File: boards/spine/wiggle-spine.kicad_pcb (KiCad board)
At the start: 2 copper layers, 114.3 x 88.9 mm, 187 parts, among them CON1 USB-B, CON2 XLR-3 Female, CON3 USB-A, CON4 2.5mm 5-24V 5A, CON5 5-24V 16A, CON6 PLR135, CON7 PLT133, Q1 DMN3190LDW, Q2 2N7002P, Q3 AOD4189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

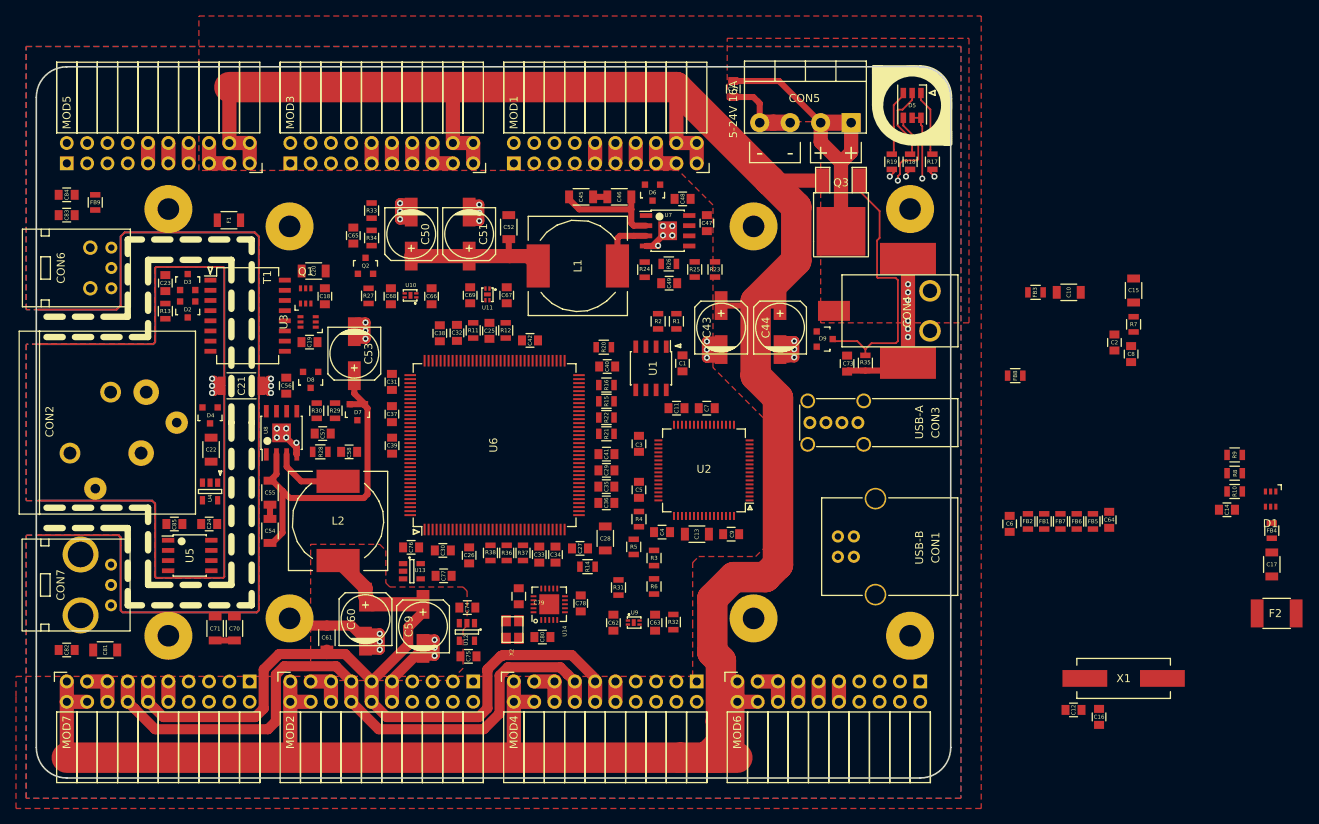
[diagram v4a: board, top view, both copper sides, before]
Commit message: Working on module power routing
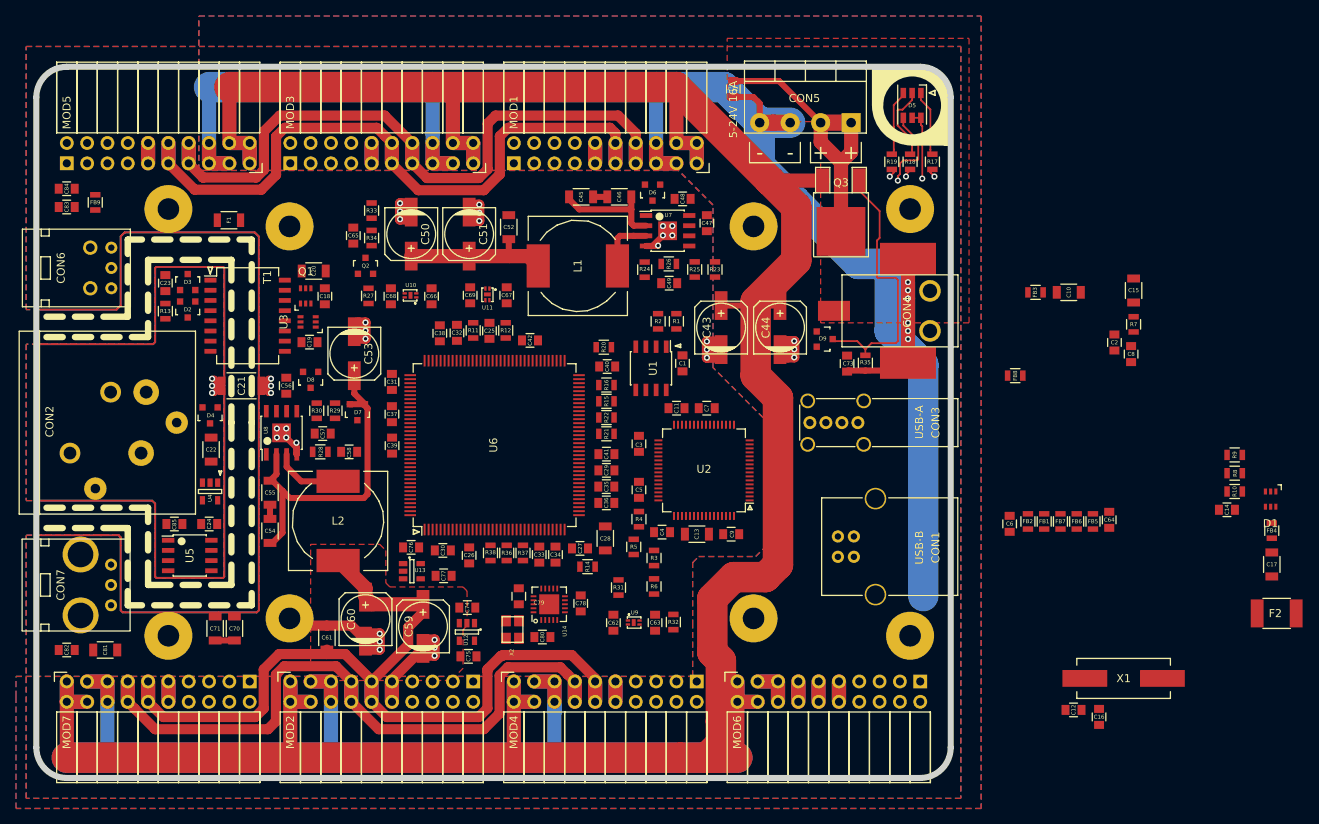
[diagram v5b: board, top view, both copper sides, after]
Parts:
- moved C83 1.02 mm to (88.9, 59.4)
- moved C84 0.76 mm to (88.9, 57.1)
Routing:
- net GNDPWR: track 67.1 -> 384.5 mm
- net +5V: track 143.5 -> 234.8 mm
- net +3V3: track 127.0 -> 217.9 mm
- net +24V: track 358.6 -> 394.2 mm
- net GND: track 348.3 -> 365.6 mm
- net /Power/5-24V Power Input/POWER_IN: track 37.3 -> 41.1 mm
- net /DMX512/DMXGND: track 217.7 -> 216.7 mm
- added copper zone on B.Cu, net GNDPWR
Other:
- net class Default: clearance 0.254 -> 0.1524
- rule trace_clearance: 0.254 -> 0.1524

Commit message: More power routing, mounting hole tweak, DRC
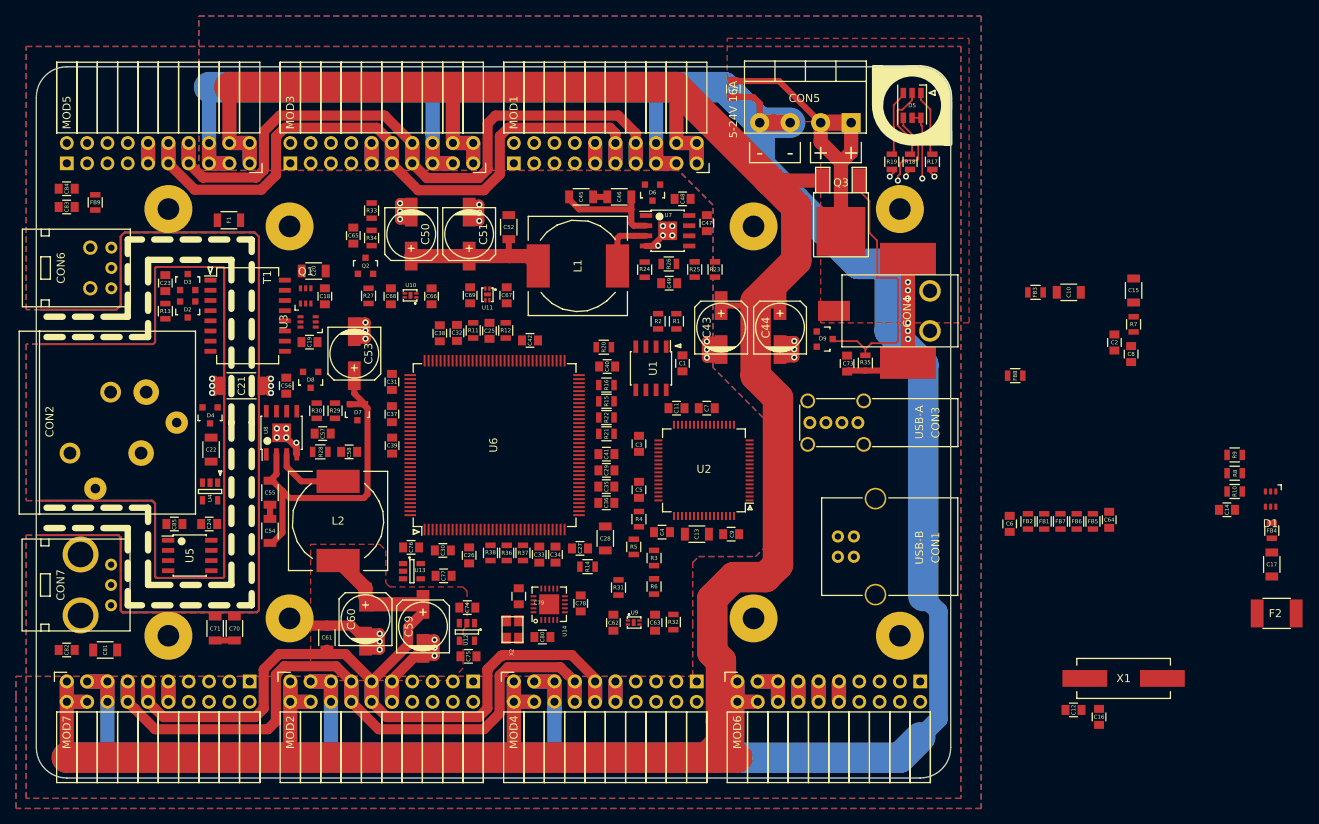
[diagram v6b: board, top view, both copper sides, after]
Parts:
- moved REF** 1.27 mm to (193.0, 113.0)
- moved REF** 1.27 mm to (193.0, 59.7)
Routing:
- net GNDPWR: track 384.5 -> 427.8 mm
- net GND: track 365.6 -> 365.1 mm

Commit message: DRC tweak, 0.2mm clearance
This is the largest we can get away with, due to the TDFN4 footprint. It's a litlte over 7 mils, which is over oshpark's 6 mil minimum.
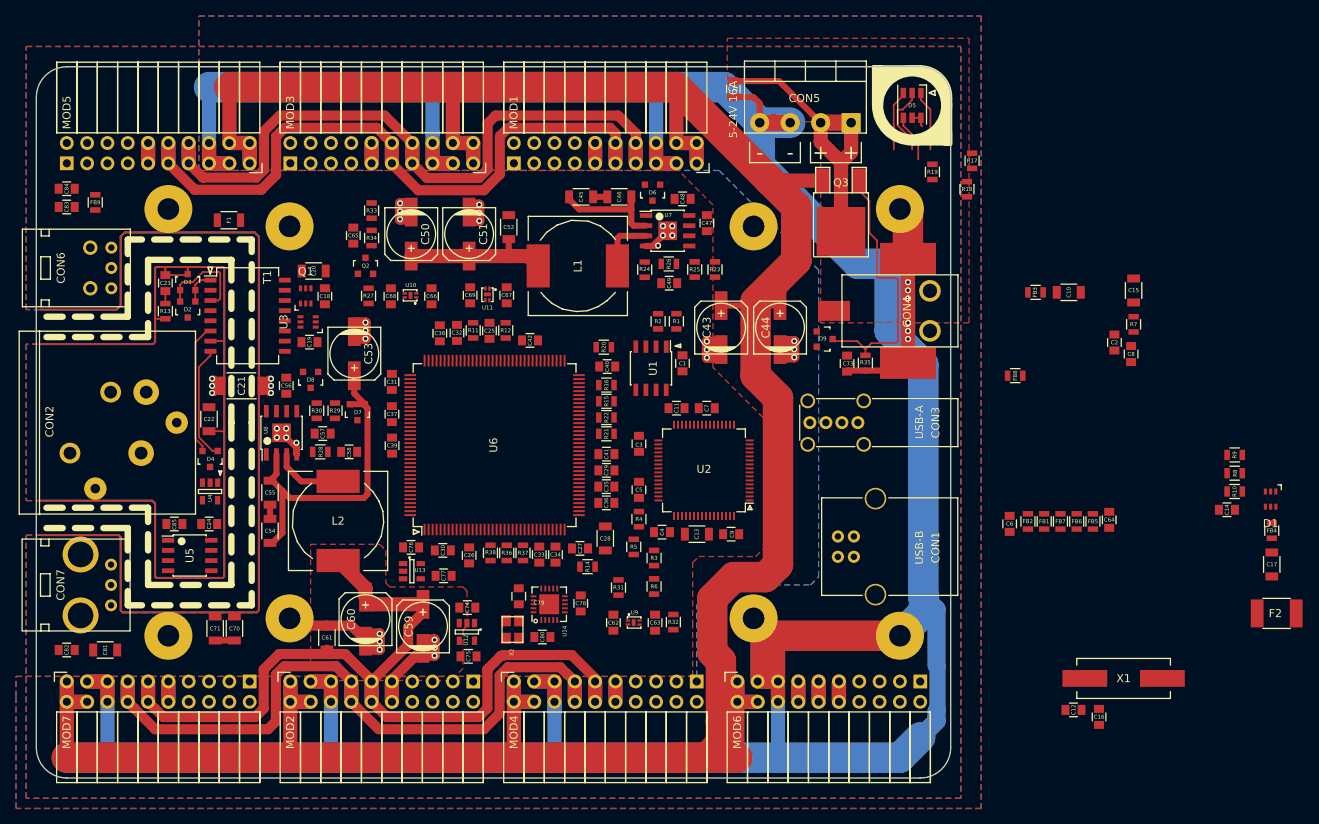
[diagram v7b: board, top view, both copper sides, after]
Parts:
- moved R18 7.90 mm to (201.4, 57.2)
- moved D4 5.44 mm to (106.8, 90.9)
- moved R19 5.24 mm to (197.1, 55.1)
- moved R17 4.95 mm to (202.1, 53.7)
- moved C22 3.82 mm to (106.7, 86.0), turned to 270 degrees
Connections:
- REF** pad 1: (no net) -> GNDPWR (x3)
- REF** pad 1: GND -> GNDPWR
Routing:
- net GNDPWR: track 427.8 -> 508.3 mm
- net Net-(D4-Pad2): track 0.00 -> 16.4 mm
- net Net-(D4-Pad1): track 0.00 -> 14.4 mm
- net Net-(D2-Pad2): track 0.00 -> 12.3 mm
- net /DMX512/DMXGND: track 216.7 -> 226.4 mm
- net +5V: track 234.8 -> 228.3 mm, vias 1 -> 0
- net Net-(D2-Pad1): track 0.00 -> 4.88 mm
- net +3V3: track 217.9 -> 213.1 mm, vias 1 -> 0
- net Net-(C23-Pad1): track 0.00 -> 1.86 mm
- net /FPGA/GREEN_N: track 1.28 -> 0.00 mm, vias 1 -> 0
- net /FPGA/BLUE_N: track 1.10 -> 0.00 mm, vias 1 -> 0
- net /FPGA/RED_N: track 1.10 -> 0.00 mm, vias 1 -> 0
- net Net-(D5-Pad2): track 9.47 -> 8.89 mm
- net Net-(D5-Pad3): track 8.15 -> 7.57 mm
- net Net-(D5-Pad1): track 8.14 -> 7.56 mm
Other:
- net class Default: clearance 0.1524 -> 0.2
- rule pad_to_mask_clearance: 0.254 -> 0.2
- rule trace_clearance: 0.1524 -> 0.2

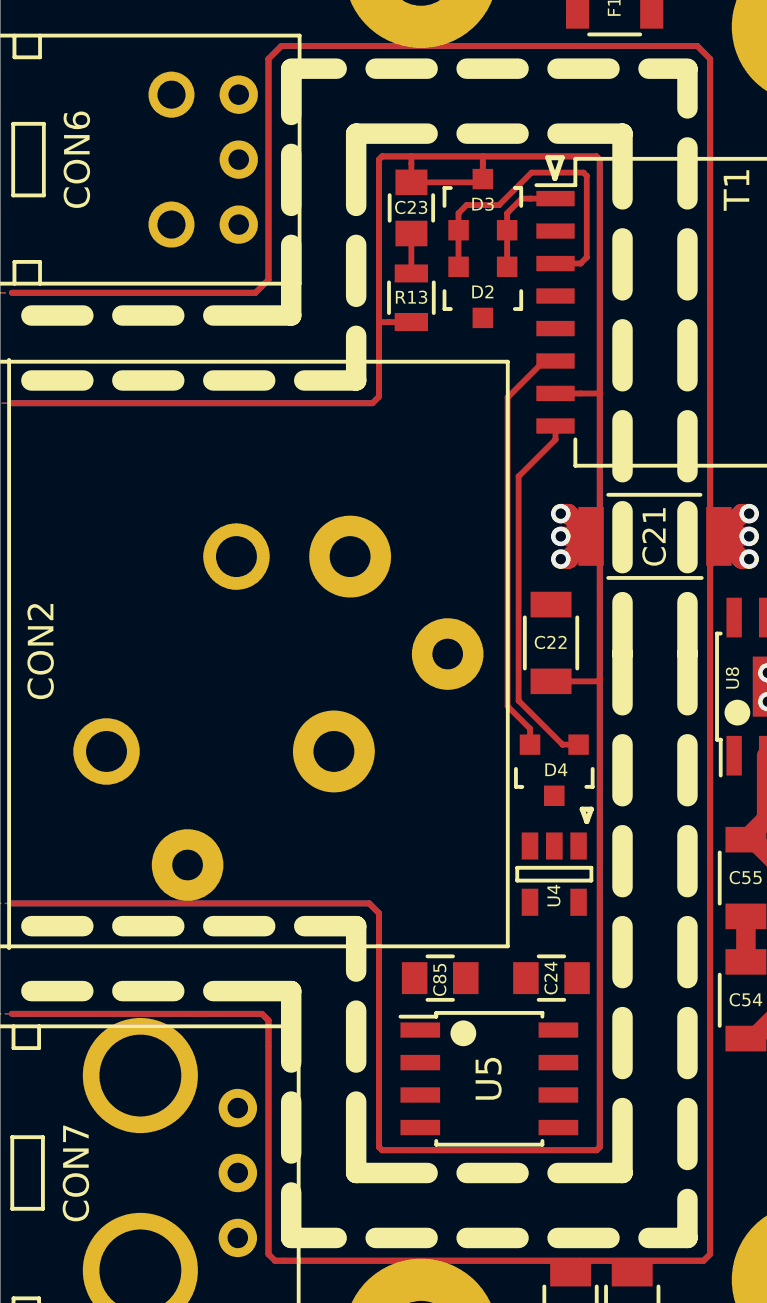
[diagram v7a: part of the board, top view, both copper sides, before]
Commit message: DMX secondary routed
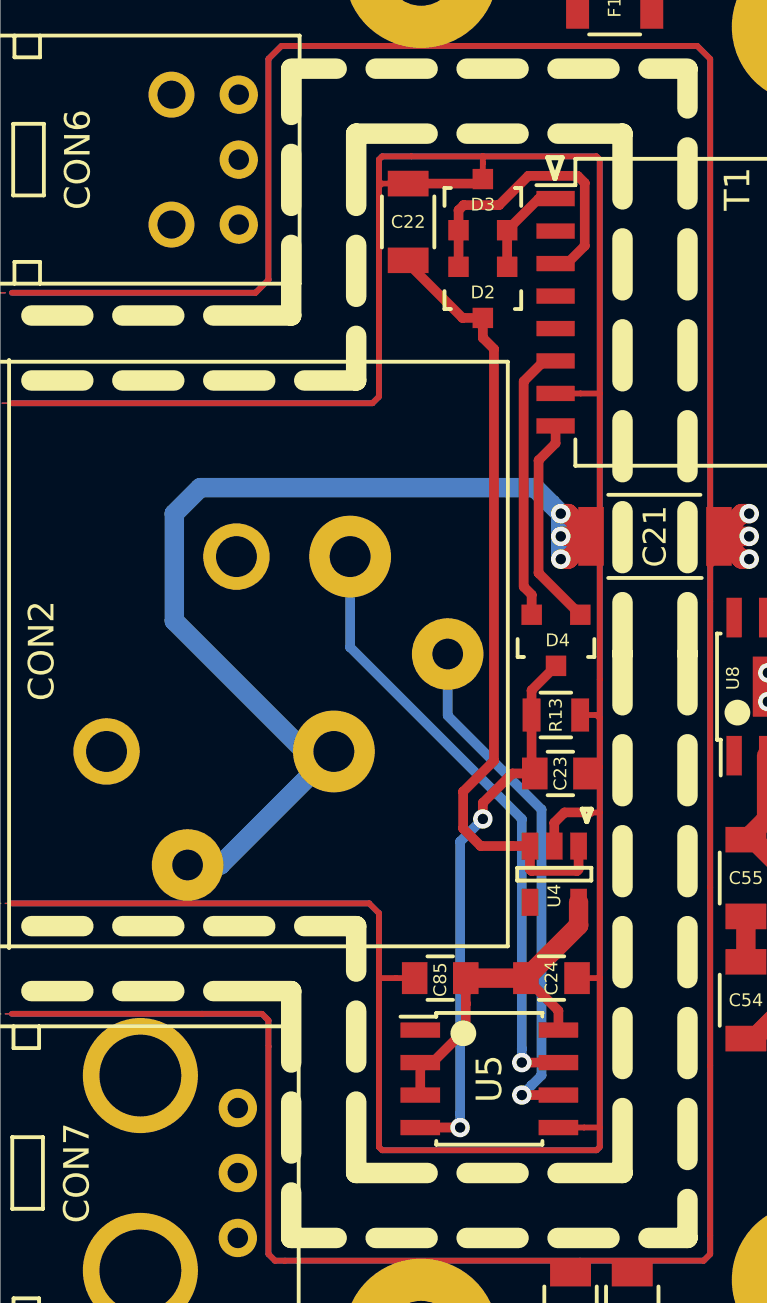
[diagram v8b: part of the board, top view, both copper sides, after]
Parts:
- moved C23 22.9 mm to (107.0, 91.1), turned to 0 degrees
- moved C22 17.4 mm to (101.1, 69.5), turned to 90 degrees
- moved R13 17.3 mm to (106.9, 88.8), turned to 180 degrees
- moved D4 5.08 mm to (106.9, 85.9)
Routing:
- net /DMX512/DMXGND: track 226.4 -> 269.8 mm
- net Net-(C22-Pad1): track 0.00 -> 31.2 mm
- net Net-(CON2-Pad2): track 0.00 -> 24.0 mm, vias 0 -> 1
- net Net-(CON2-Pad3): track 0.00 -> 20.5 mm, vias 0 -> 1
- net Net-(C23-Pad1): track 1.86 -> 21.8 mm, vias 0 -> 2
- net Net-(C24-Pad1): track 0.00 -> 15.0 mm
- net Net-(D4-Pad1): track 14.4 -> 8.33 mm
- net Net-(D4-Pad2): track 16.4 -> 10.8 mm
- net Net-(D2-Pad2): track 12.3 -> 11.7 mm
